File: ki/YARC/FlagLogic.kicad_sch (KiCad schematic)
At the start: 11 parts, among them U105 74LS86, U106 74LS139, U107 74HC00, U108 74HC02, U109 74LS32, U110 74LS21, U111 74LS153, U112 74LS573, U113 74LS573, U114 74LS574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

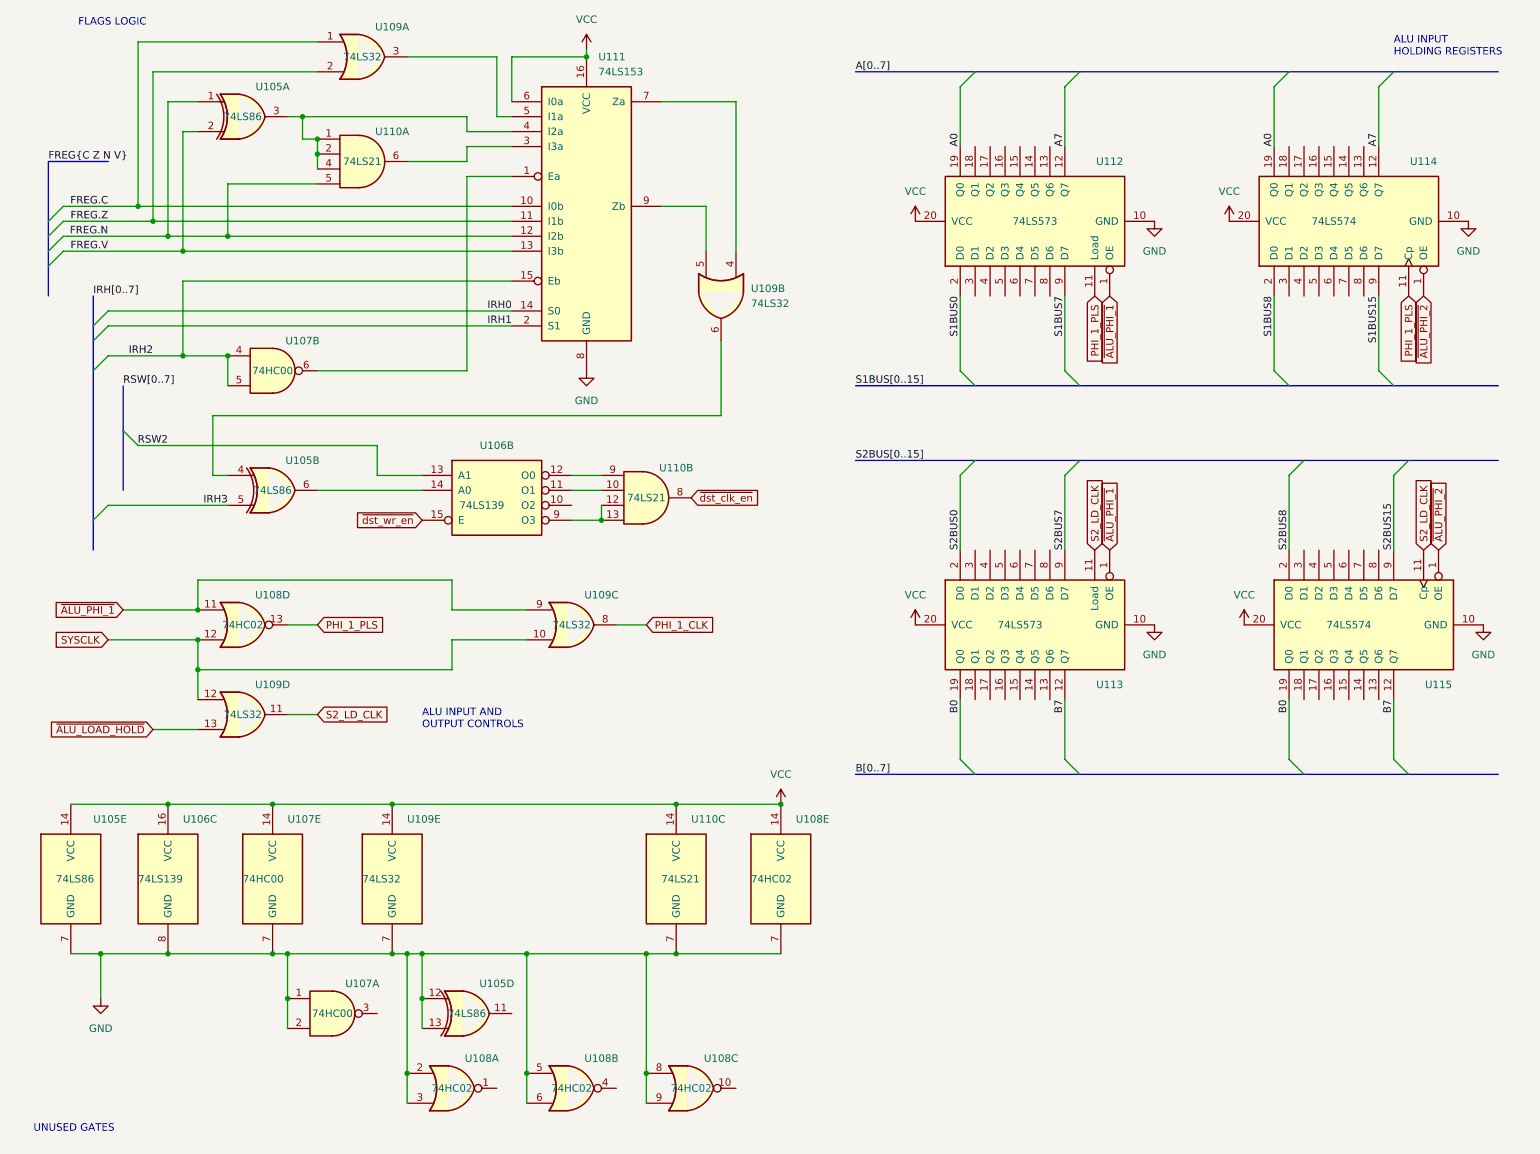
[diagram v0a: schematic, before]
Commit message: Yet more cleanup on ALU and flags design
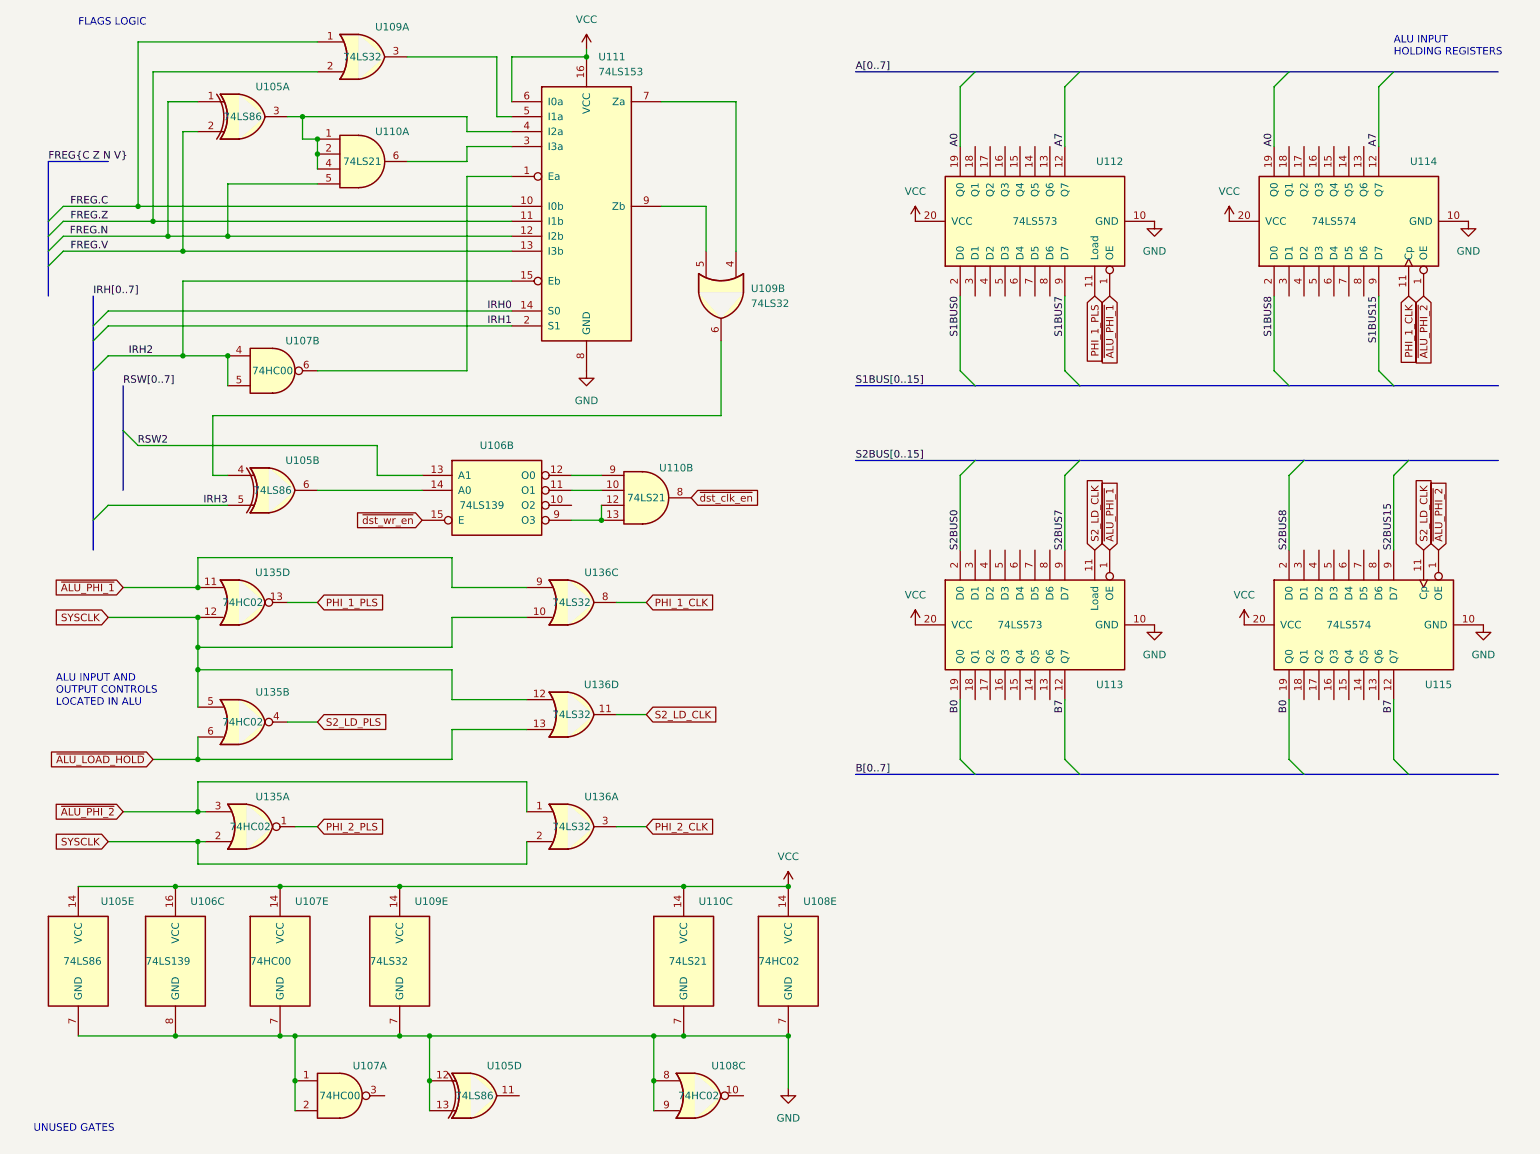
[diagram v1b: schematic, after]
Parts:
- removed unit 1 of U108
- removed unit 2 of U108
- added unit 1 of U135
- added unit 2 of U135
- added unit 1 of U136
- renumbered U108 to U135, U109 to U136
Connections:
- net PHI_1_CLK: now also U114.11 (Cp)
- net PHI_1_PLS: no longer U114.11 (Cp)
- net SYSCLK: now also U135.2, U135.5, U136.2
- net ~{ALU_LOAD_HOLD}: now also U135.6
- net ~{ALU_PHI_2}: now also U135.3, U136.1
- new net PHI_2_CLK: U136.3
- new net PHI_2_PLS: U135.1
- new net S2_LD_PLS: U135.4
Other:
- note added: "ALU INPUT AND OUTPUT CONTROLS LOCATED IN ALU"
- note removed: "ALU INPUT AND OUTPUT CONTROLS"
- moved on the sheet: U105D, U105E, U106C, U107A, U107E, U108C, U108E, U109E, U110C, U135D, U136C, U136D

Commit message: Ongoing corrections and improvements
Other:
- moved on the sheet: U105D, U105E, U106C, U107A, U107E, U108C, U108E, U109E, U110C, U135A, U136A

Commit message: Add the ACN mini-bus which can come from the instruction bits 11:8 or from the microcode bits 23:20. It selects the ALU operation and the condition codes.
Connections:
- net IRH0 renamed ACN0
- net IRH1 renamed ACN1
- net IRH2 renamed ACN2
- net IRH3 renamed ACN3
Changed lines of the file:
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@@
+    (effects (font (size 1.27 1.27)) (justify left bottom))
+  )
+  (label "ACN[0..3]" (at 22.86 60.96 0)
+    (effects (font (size 1.27 1.27)) (justify left bottom))
+  )
+  (label "ACN3" (at 25.4 96.52 0)
     (effects (font (size 1.27 1.27)) (justify left bottom))
   )
@@
   )
   (label "RSW2" (at 35.56 86.36 180)
-    (effects (font (size 1.27 1.27)) (justify right bottom))
-  )
-  (label "IRH3" (at 45.72 96.52 180)
     (effects (font (size 1.27 1.27)) (justify right bottom))
   )
@@
     (effects (font (size 1.27 1.27)) (justify left bottom))
   )
-  (label "IRH1" (at 93.98 66.04 180)
-    (effects (font (size 1.27 1.27)) (justify right bottom))
-  )
   (label "FREG.C" (at 25.4 45.72 180)
     (effects (font (size 1.27 1.27)) (justify right bottom))
@@
     (effects (font (size 1.27 1.27)) (justify left bottom))
   )
-  (label "IRH0" (at 93.98 63.5 180)
+  (label "B7" (at 187.96 129.54 270)
     (effects (font (size 1.27 1.27)) (justify right bottom))
   )
-  (label "B7" (at 187.96 129.54 270)
-    (effects (font (size 1.27 1.27)) (justify right bottom))
+  (label "ACN2" (at 25.4 71.12 0)
+    (effects (font (size 1.27 1.27)) (justify left bottom))
   )
   (label "S2BUS7" (at 187.96 104.14 90)
@@
     (effects (font (size 1.27 1.27)) (justify left bottom))
   )
-  (label "IRH2" (at 33.02 71.12 180)
-    (effects (font (size 1.27 1.27)) (justify right bottom))
-  )
-  (label "IRH[0..7]" (at 22.86 60.96 0)
+  (label "ACN0" (at 25.4 63.5 0)
     (effects (font (size 1.27 1.27)) (justify left bottom))
   )
@@
     (effects (font (size 1.27 1.27)) (justify right bottom))
   )
+  (label "ACN1" (at 25.4 66.04 0)
+    (effects (font (size 1.27 1.27)) (justify left bottom))
+  )
   (label "B0" (at 226.06 129.54 270)

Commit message: Correct unit numbers on 7486 in Flags section
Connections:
- net ACN3: now also U105.10; no longer U105.5
- net FREG.N: now also U105.12; no longer U105.1
- net FREG.V: now also U105.13; no longer U105.2
- net GND: now also U105.1, U105.2; no longer U105.12, U105.13
- net at U109.6: now also U105.9; no longer U105.4
- net at U106.14 (A0): now also U105.8; no longer U105.6
- net at U110.1, U110.2, U110.4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: now also U105.11; no longer U105.3
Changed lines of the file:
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@@
     )
   )
-  (symbol (lib_id "74xx:74LS86") (at 53.34 93.98 0) (unit 2)
+  (symbol (lib_id "74xx:74LS86") (at 53.34 93.98 0) (unit 3)
     (in_bom yes) (on_board yes)
     (property "Reference" "U105" (id 0) (at 58.42 88.9 0))
@@
       (effects (font (size 1.27 1.27)) hide)
     )
-    (pin "4")
-    (pin "5")
-    (pin "6")
+    (pin "10")
+    (pin "8")
+    (pin "9")
   )
   (symbol (lib_id "74xx:74LS32") (at 68.58 20.32 0) (unit 1)
@@
     (pin "9")
   )
-  (symbol (lib_id "74xx:74LS86") (at 88.9 198.12 0) (unit 4)
+  (symbol (lib_id "74xx:74LS86") (at 88.9 198.12 0) (unit 1)
     (in_bom yes) (on_board yes)
     (property "Reference" "U105" (id 0) (at 93.98 193.04 0))
@@
       (effects (font (size 1.27 1.27)) hide)
     )
-    (pin "11")
-    (pin "12")
-    (pin "13")
+    (pin "1")
+    (pin "2")
+    (pin "3")
   )
   (symbol (lib_id "power:GND") (at 142.24 196.85 0) (unit 1)
@@
     (pin "1")
   )
-  (symbol (lib_id "74xx:74LS86") (at 48.26 30.48 0) (unit 1)
+  (symbol (lib_id "74xx:74LS86") (at 48.26 30.48 0) (unit 4)
     (in_bom yes) (on_board yes)
     (property "Reference" "U105" (id 0) (at 53.34 25.4 0))
@@
       (effects (font (size 1.27 1.27)) hide)
     )
-    (pin "1")
-    (pin "2")
-    (pin "3")
+    (pin "11")
+    (pin "12")
+    (pin "13")
   )
   (symbol (lib_id "74xx:74LS21") (at 116.84 95.25 0) (unit 2)

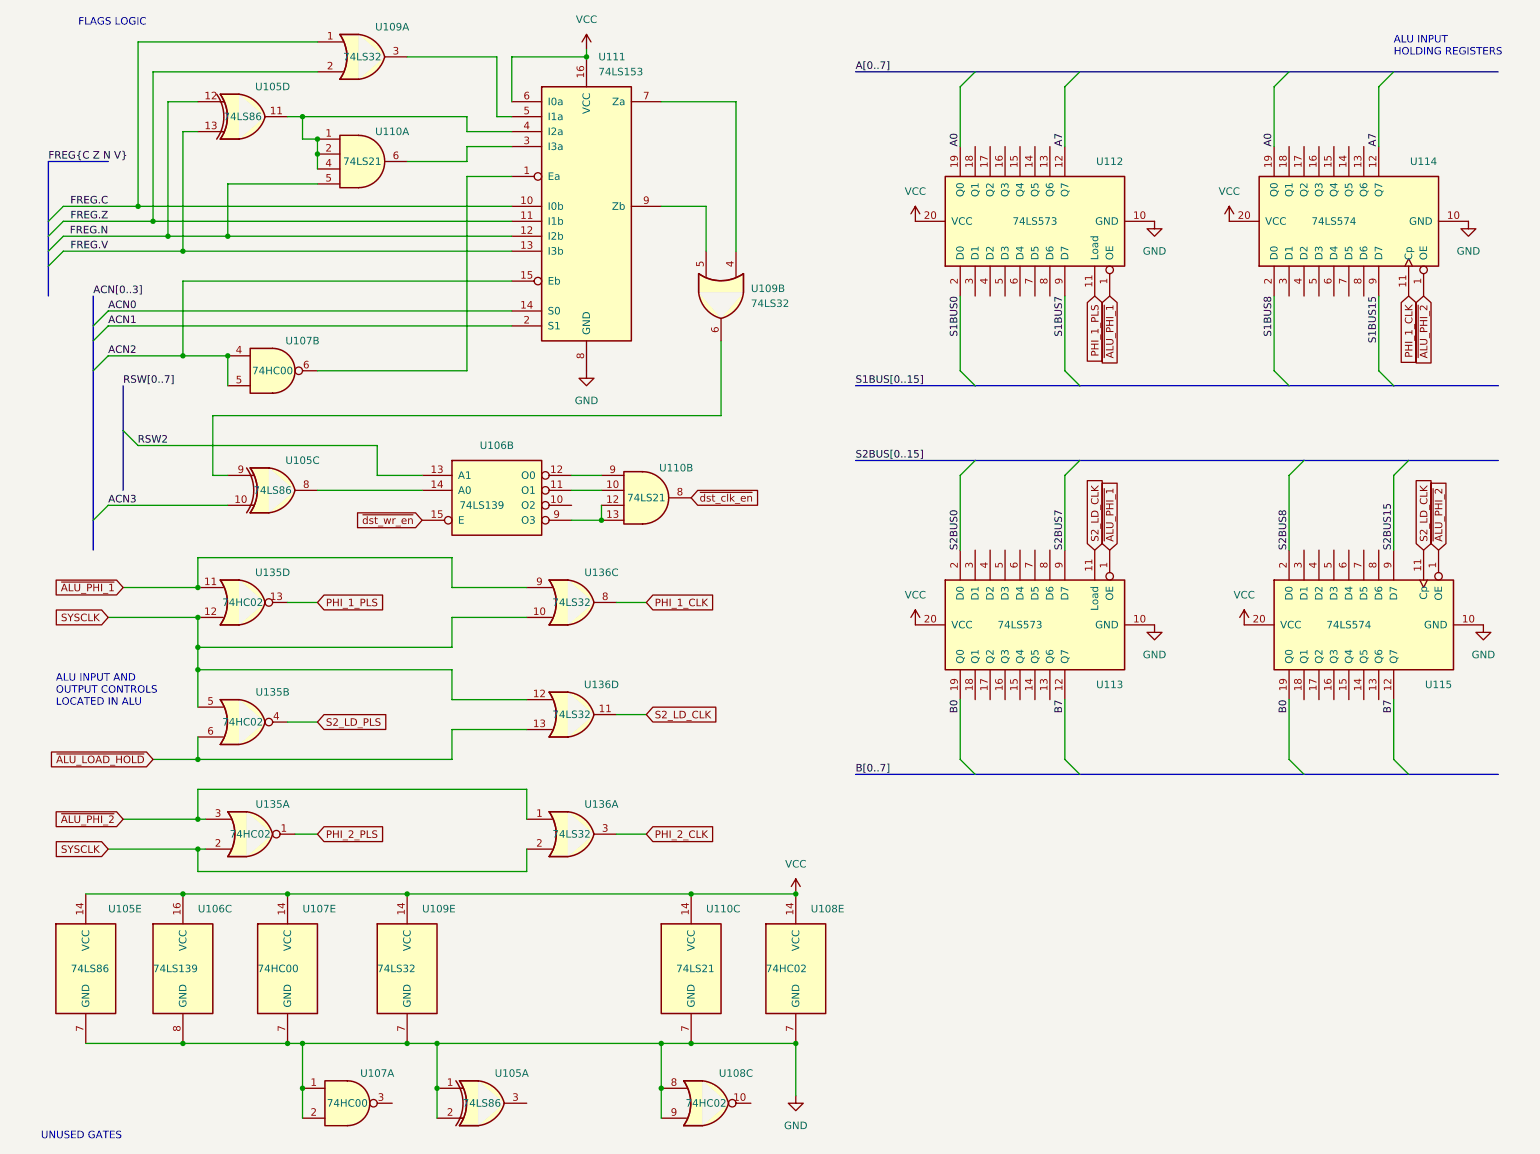
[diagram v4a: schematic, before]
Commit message: Fix schematic error in <= gate. Cleanup signal naming. Fix subtle issue with carry in signal.
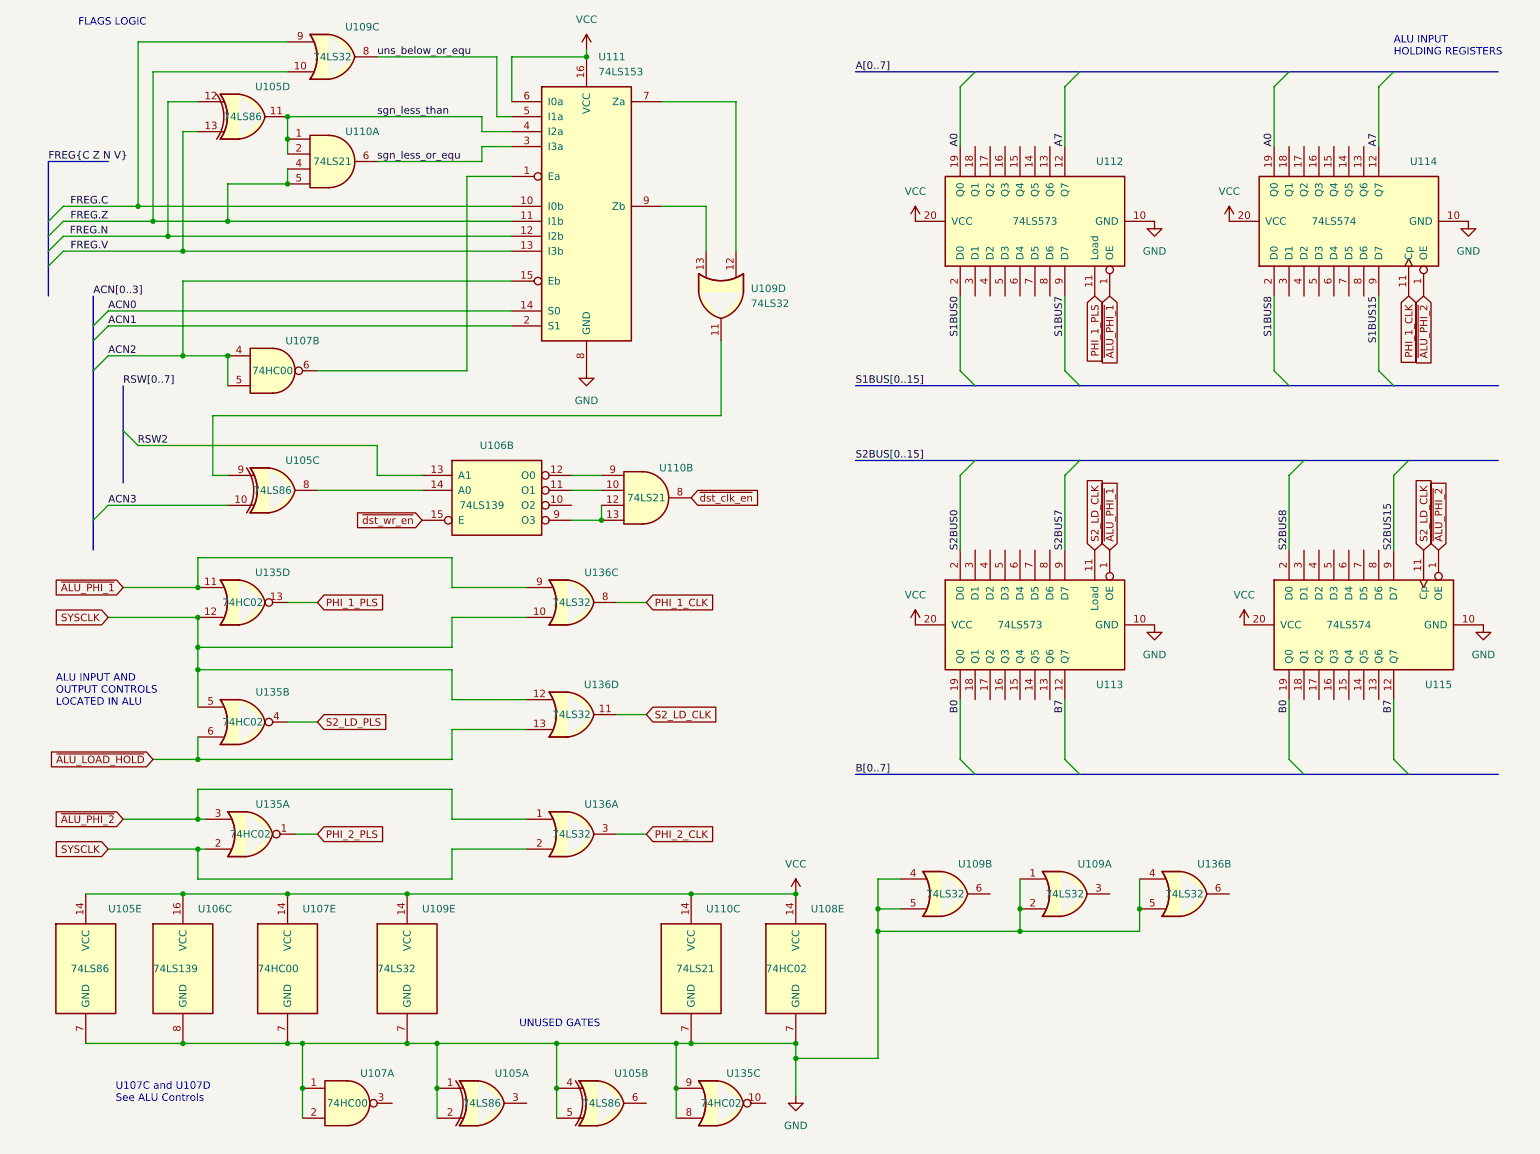
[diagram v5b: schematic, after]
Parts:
- removed unit 3 of U108
- added unit 2 of U105
- added unit 2 of U109
- added unit 1 of U109
- added unit 3 of U135
- added unit 2 of U136
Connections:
- net FREG.C: now also U109.9; no longer U109.1
- net FREG.N: no longer U110.5
- net FREG.Z: now also U109.10, U110.4, U110.5; no longer U109.2
- net GND: now also U105.4, U105.5, U109.1, U109.2, U109.4, U109.5, U135.8, U135.9, U136.4, U136.5
- net at U105.9: now also U109.11; no longer U109.6
- net uns_below_or_equ: now reaches U111.5 (I1a)
- net uns_below_or_equ: now also U109.8; no longer U109.3
- net sgn_less_than: now reaches U105.11, U110.1, U110.2, U111.4 (I2a)
- net sgn_less_than: no longer U110.4
- net sgn_less_or_equ: now reaches U110.6, U111.3 (I3a)
- net at U111.7 (Za): now also U109.12; no longer U109.4
- net at U111.9 (Zb): now also U109.13; no longer U109.5
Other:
- note added: "U107C and U107D See ALU Controls"
- moved on the sheet: U109C, U110A
